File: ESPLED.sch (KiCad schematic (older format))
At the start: 24 parts, among them CON1 BARREL_JACK, J1 USB_B_Micro, P2 LED_CON, P3 LED_CON_SCREW, P4 LED_CON_SCREW, Q1 IRLZ34N, Q2 IRLZ34N, Q3 IRLZ34N, SW1 Reset, SW2 Program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

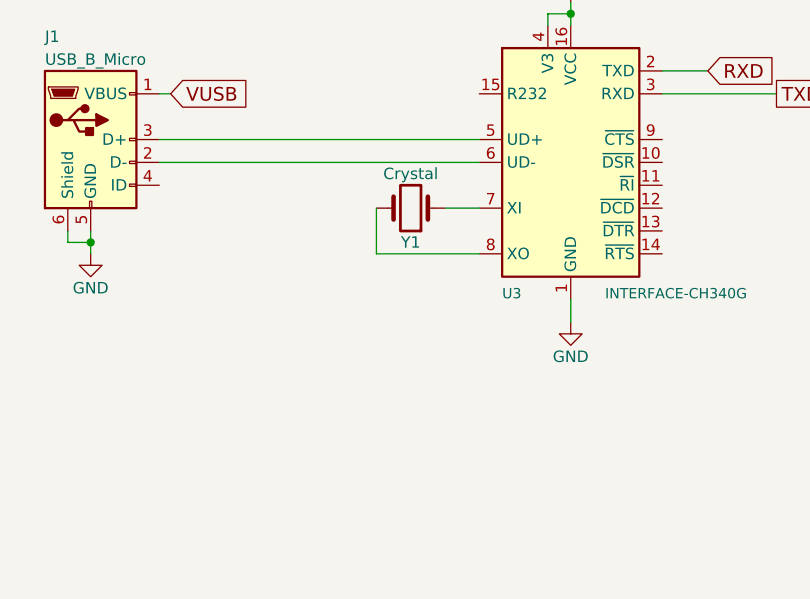
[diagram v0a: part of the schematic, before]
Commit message: Added caps for crystal
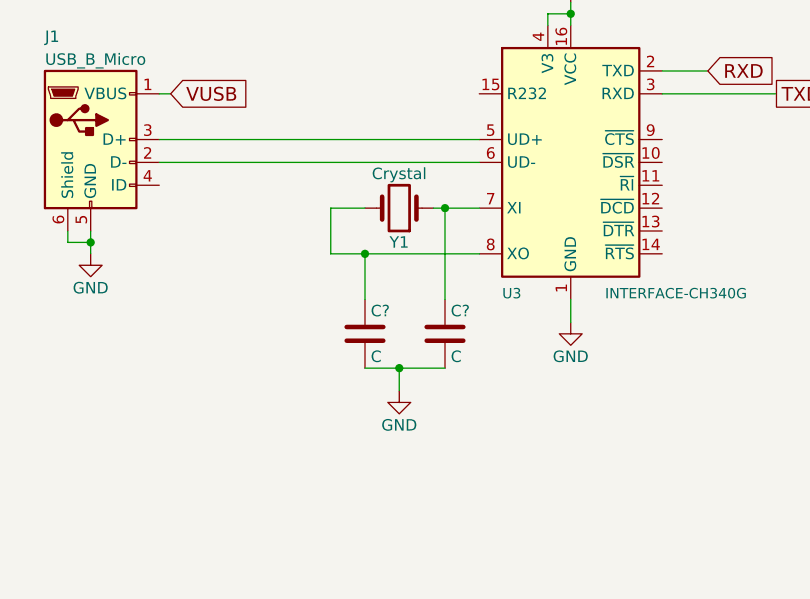
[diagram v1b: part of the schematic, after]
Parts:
- added C? (x2): C, symbol C
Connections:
- net GND: now also C?.2, C?.2
- net at U3.7 (XI), Y1.1: now also C?.1
- net at U3.8 (XO), Y1.2: now also C?.1
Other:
- moved on the sheet: Y1
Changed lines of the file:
@@
 L Crystal Y1
 U 1 1 5BF93CC5
-P 8450 2200
-F 0 "Y1" H 8450 2350 50  0000 C CNN
-F 1 "Crystal" H 8450 2050 50  0000 C CNN
-F 2 "Crystal:Crystal_SMD_0603-2Pin_6.0x3.5mm_HandSoldering" H 8450 2200 50  0001 C CNN
-F 3 "" H 8450 2200 50  0001 C CNN
-	1    8450 2200
+P 8400 2200
+F 0 "Y1" H 8400 2350 50  0000 C CNN
+F 1 "Crystal" H 8400 2050 50  0000 C CNN
+F 2 "Crystal:Crystal_SMD_0603-2Pin_6.0x3.5mm_HandSoldering" H 8400 2200 50  0001 C CNN
+F 3 "" H 8400 2200 50  0001 C CNN
+	1    8400 2200
 	-1   0    0    1
 $EndComp
@@
 Connection ~ 9150 1350
 Wire Wire Line
-	8600 2200 8750 2200
-Wire Wire Line
-	8300 2200 8300 2400
-Wire Wire Line
-	8300 2400 8750 2400
-Wire Wire Line
 	6950 2350 7050 2350
 Wire Wire Line
@@
 Wire Wire Line
 	9150 2600 9150 2700
+$Comp
+L C C?
+U 1 1 5BFBCF59
+P 8250 2750
+F 0 "C?" H 8275 2850 50  0000 L CNN
+F 1 "C" H 8275 2650 50  0000 L CNN
+F 2 "" H 8288 2600 50  0001 C CNN
+F 3 "" H 8250 2750 50  0001 C CNN
+	1    8250 2750
+	1    0    0    -1
+$EndComp
+$Comp
+L C C?
+U 1 1 5BFBD323
+P 8600 2750
+F 0 "C?" H 8625 2850 50  0000 L CNN
+F 1 "C" H 8625 2650 50  0000 L CNN
+F 2 "" H 8638 2600 50  0001 C CNN
+F 3 "" H 8600 2750 50  0001 C CNN
+	1    8600 2750
+	1    0    0    -1
+$EndComp
+Wire Wire Line
+	8600 2200 8600 2600
+Wire Wire Line
+	8550 2200 8750 2200
+Wire Wire Line
+	8250 2200 8100 2200
+Wire Wire Line
+	8100 2200 8100 2400
+Wire Wire Line
+	8100 2400 8750 2400
+Connection ~ 8600 2200
+Wire Wire Line
+	8250 2600 8250 2400
+Connection ~ 8250 2400
+Wire Wire Line
+	8250 2900 8600 2900
+$Comp
+L GND #PWR?
+U 1 1 5BFBD9E2
+P 8400 3000
+F 0 "#PWR?" H 8400 2750 50  0001 C CNN
+F 1 "GND" H 8400 2850 50  0000 C CNN
+F 2 "" H 8400 3000 50  0001 C CNN
+F 3 "" H 8400 3000 50  0001 C CNN
+	1    8400 3000
+	1    0    0    -1
+$EndComp
+Wire Wire Line
+	8400 2900 8400 3000
+Connection ~ 8400 2900
 $EndSCHEMATC

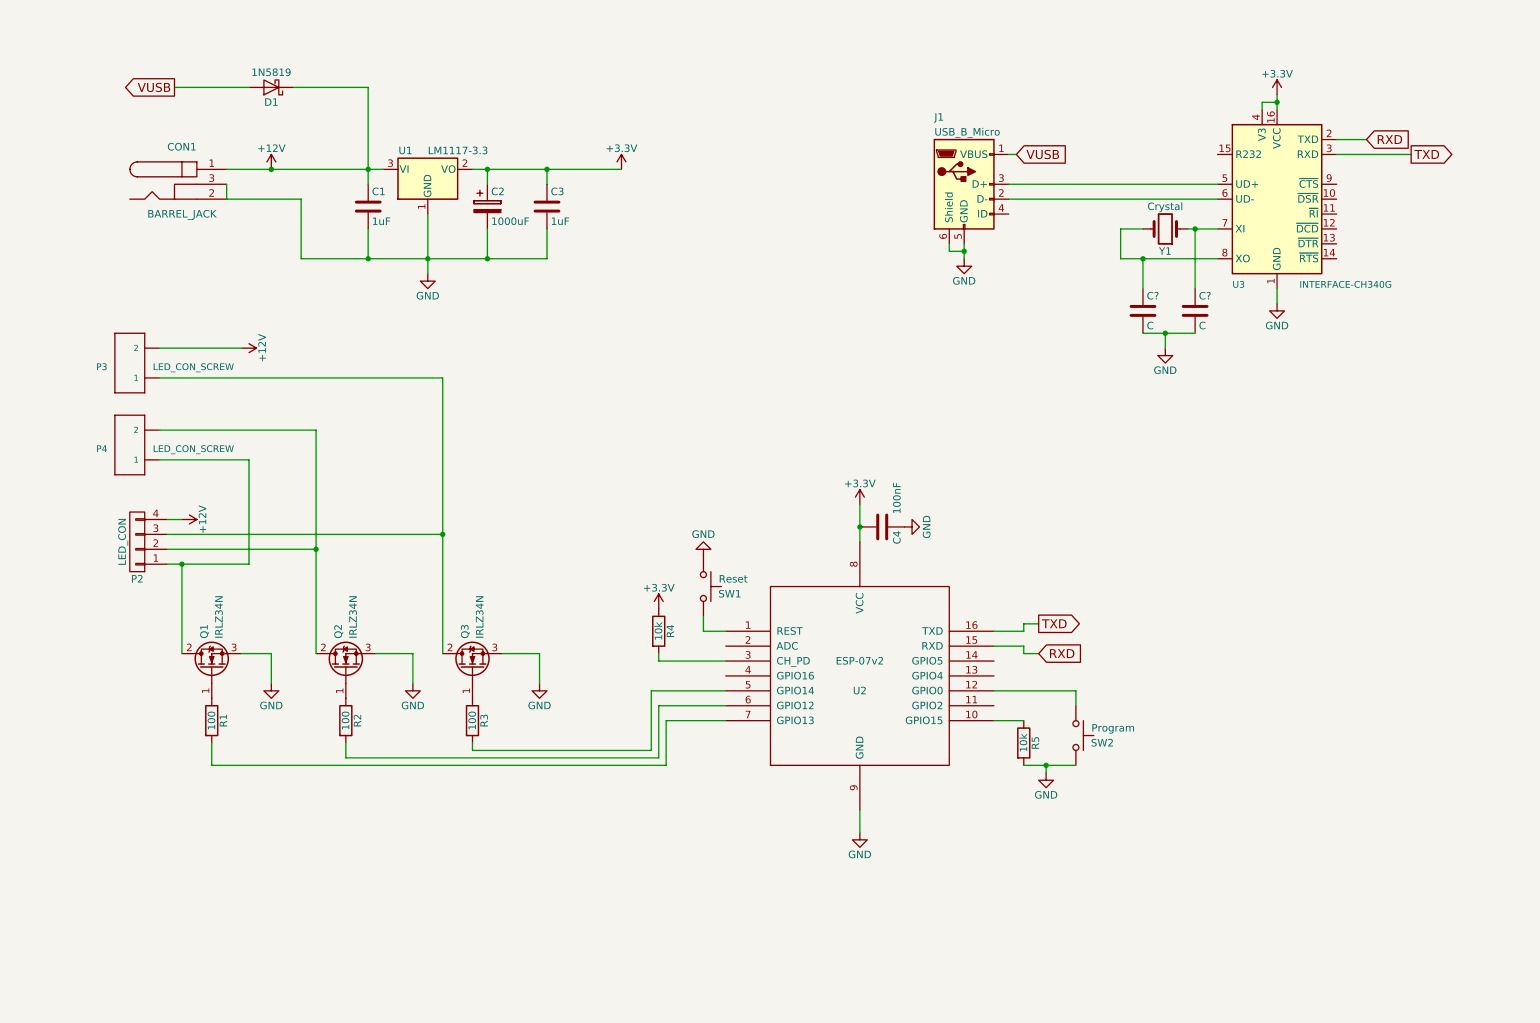
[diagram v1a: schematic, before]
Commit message: Schematic done. Next: Fottprint research
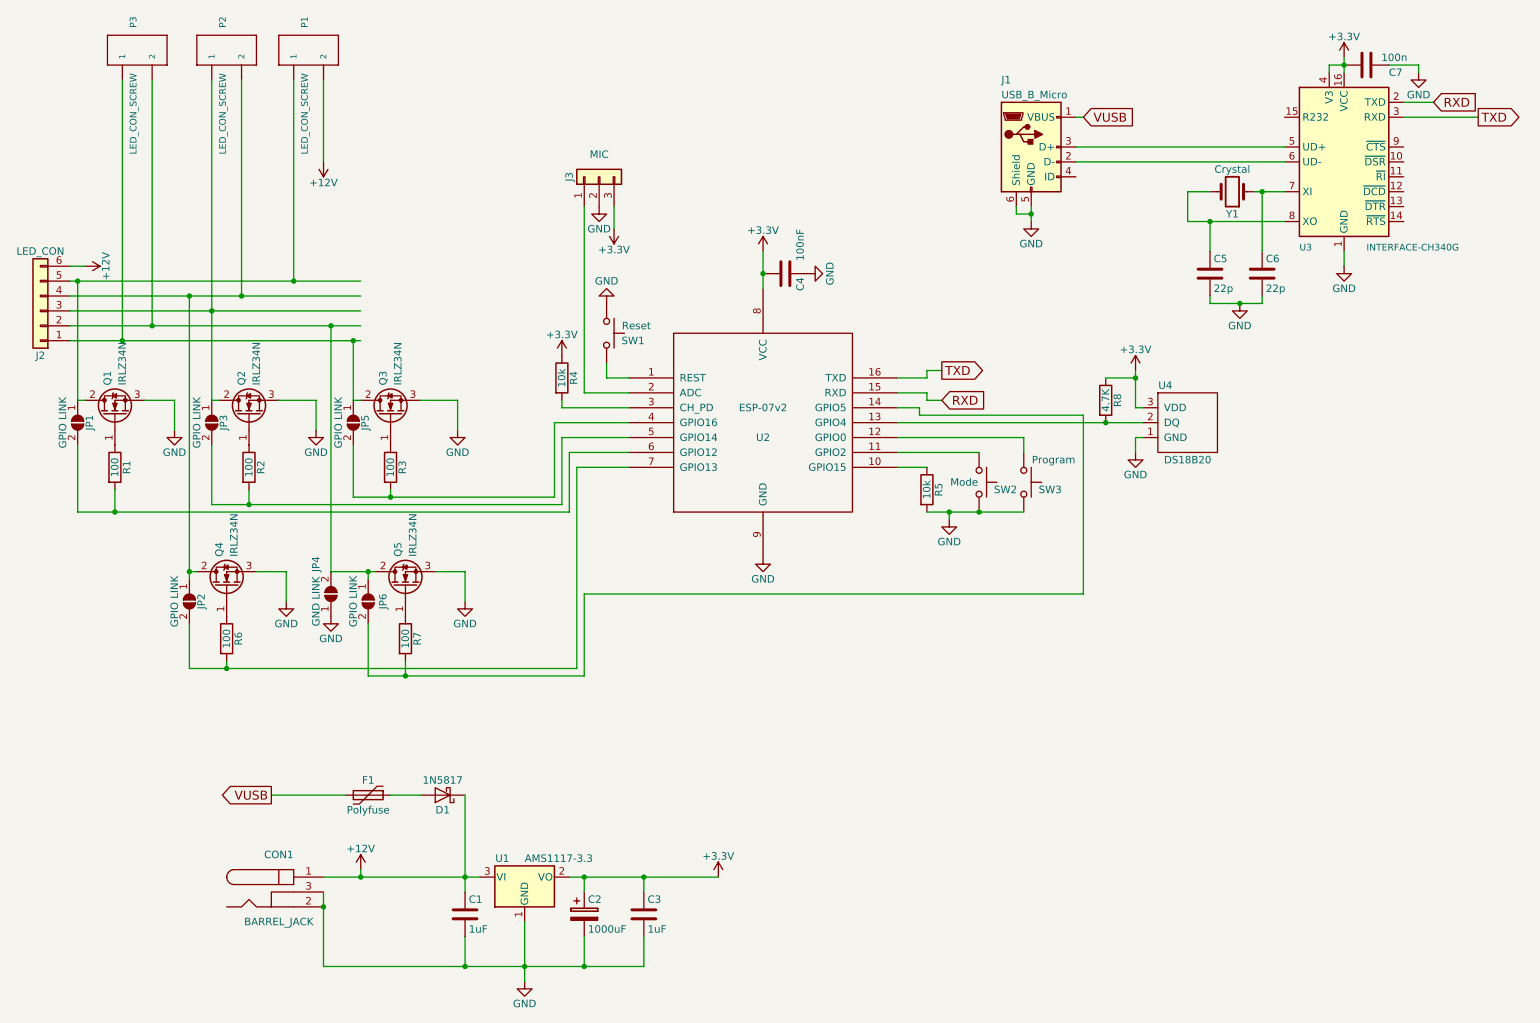
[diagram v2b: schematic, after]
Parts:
- removed D1: 1N5819, Diode_THT:D_DO-41_SOD81_P7.62mm_Horizontal, symbol 1N5819
- removed P2: LED_CON, Pin_Headers:Pin_Header_Straight_1x04_Pitch2.54mm, symbol CONN_01X04
- removed U1: LM1117-3.3, Power_Integrations:TO-220, symbol LM1117-3.3
- added C7: 100n, symbol C
- added D1: 1N5817, Diodes_THT:D_DO-41_SOD81_Horizontal_RM10, symbol 1N5817
- added F1: Polyfuse, symbol Polyfuse
- added J2: LED_CON, symbol Conn_01x06
- added J3: MIC, symbol Conn_01x03
- added JP1, JP2, JP3, JP5, JP6: GPIO LINK, symbol SolderJumper_2_Open
- added JP4: GND LINK, symbol SolderJumper_2_Open
- added P2: LED_CON_SCREW, SeeedOPL-Connector:H2-3.5-7.0X7.0MM, symbol SCREW-TERMINAL-GREEN_2P-3.5_
- added Q4, Q5: IRLZ34N, TO_SOT_Packages_THT:TO-220_Horizontal, symbol IRLZ34N
- added R6, R7: 100, Resistors_SMD:R_0603_HandSoldering, symbol R
- added R8: 4.7K, symbol R
- added SW3: Program, Button_Switch_THT:SW_PUSH_6mm_H5mm, symbol SW_Push
- added U1: AMS1117-3.3, Package_TO_SOT_SMD:SOT-223-3_TabPin2, symbol AMS1117-3.3
- added U4: DS18B20, symbol DS18B20
- C5, C6: renamed from C?; value C -> 22p
- SW2: value Program -> Mode
- renumbered P3 to P1, P4 to P3
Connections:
- wire segments 83 -> 125
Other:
- moved on the sheet: C1, C2, C3, C4, C5, C6, CON1, J1, P1, P3, Q1, Q2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
